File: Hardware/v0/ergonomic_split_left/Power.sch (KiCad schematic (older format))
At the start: 3 parts, among them U9 TCR2EF33

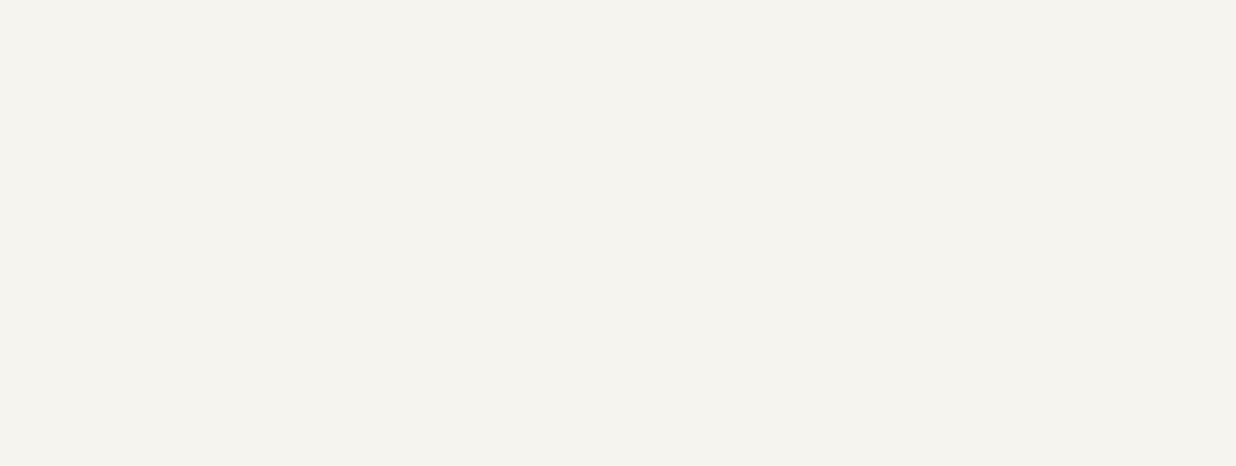
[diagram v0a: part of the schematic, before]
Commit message: Drawing board outline Basic placement done Adding rotary encoder to the switch matrix Adding mounting holes
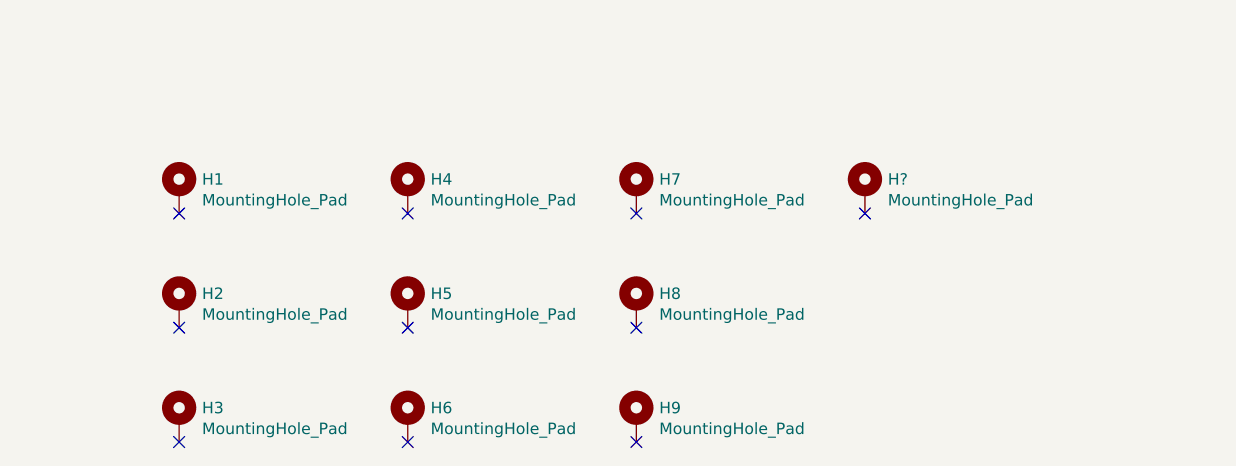
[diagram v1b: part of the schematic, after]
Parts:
- added H1, H2, H3, H4, H5, H6, H7, H8, H9, H?: MountingHole_Pad, mounting_hole:MountingHole_3.2mm_M3_ISO7380_Pad, symbol Mechanical:MountingHole_Pad
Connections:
- no-connect marks 0 -> 10
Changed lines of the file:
@@
 $Descr A4 11693 8268
 encoding utf-8
-Sheet 7 7
+Sheet 6 7
 Title "TKL Keyboard"
 Date ""
@@
 	1    0    0    -1
 $EndComp
+$Comp
+L Mechanical:MountingHole_Pad H1
+U 1 1 62F25DCF
+P 1500 5550
+F 0 "H1" H 1600 5599 50  0000 L CNN
+F 1 "MountingHole_Pad" H 1600 5508 50  0000 L CNN
+F 2 "mounting_hole:MountingHole_3.2mm_M3_ISO7380_Pad" H 1500 5550 50  0001 C CNN
+F 3 "~" H 1500 5550 50  0001 C CNN
+	1    1500 5550
+	1    0    0    -1
+$EndComp
+NoConn ~ 1500 5650
+$Comp
+L Mechanical:MountingHole_Pad H2
+U 1 1 62F281A1
+P 1500 6050
+F 0 "H2" H 1600 6099 50  0000 L CNN
+F 1 "MountingHole_Pad" H 1600 6008 50  0000 L CNN
+F 2 "mounting_hole:MountingHole_3.2mm_M3_ISO7380_Pad" H 1500 6050 50  0001 C CNN
+F 3 "~" H 1500 6050 50  0001 C CNN
+	1    1500 6050
+	1    0    0    -1
+$EndComp
+NoConn ~ 1500 6150
+$Comp
+L Mechanical:MountingHole_Pad H3
+U 1 1 62F28C3F
+P 1500 6550
+F 0 "H3" H 1600 6599 50  0000 L CNN
+F 1 "MountingHole_Pad" H 1600 6508 50  0000 L CNN
+F 2 "mounting_hole:MountingHole_3.2mm_M3_ISO7380_Pad" H 1500 6550 50  0001 C CNN
+F 3 "~" H 1500 6550 50  0001 C CNN
+	1    1500 6550
+	1    0    0    -1
+$EndComp
+NoConn ~ 1500 6650
+$Comp
+L Mechanical:MountingHole_Pad H4
+U 1 1 62F2B314
+P 2500 5550
+F 0 "H4" H 2600 5599 50  0000 L CNN
+F 1 "MountingHole_Pad" H 2600 5508 50  0000 L CNN
+F 2 "mounting_hole:MountingHole_3.2mm_M3_ISO7380_Pad" H 2500 5550 50  0001 C CNN
+F 3 "~" H 2500 5550 50  0001 C CNN
+	1    2500 5550
+	1    0    0    -1
+$EndComp
+NoConn ~ 2500 5650
+$Comp
+L Mechanical:MountingHole_Pad H5
+U 1 1 62F2B31B
+P 2500 6050
+F 0 "H5" H 2600 6099 50  0000 L CNN
+F 1 "MountingHole_Pad" H 2600 6008 50  0000 L CNN
+F 2 "mounting_hole:MountingHole_3.2mm_M3_ISO7380_Pad" H 2500 6050 50  0001 C CNN
+F 3 "~" H 2500 6050 50  0001 C CNN
+	1    2500 6050
+	1    0    0    -1
+$EndComp
+NoConn ~ 2500 6150
+$Comp
+L Mechanical:MountingHole_Pad H6
+U 1 1 62F2B322
+P 2500 6550
+F 0 "H6" H 2600 6599 50  0000 L CNN
+F 1 "MountingHole_Pad" H 2600 6508 50  0000 L CNN
+F 2 "mounting_hole:MountingHole_3.2mm_M3_ISO7380_Pad" H 2500 6550 50  0001 C CNN
+F 3 "~" H 2500 6550 50  0001 C CNN
+	1    2500 6550
+	1    0    0    -1
+$EndComp
+NoConn ~ 2500 6650
+$Comp
+L Mechanical:MountingHole_Pad H7
+U 1 1 62F2BF2F
+P 3500 5550
+F 0 "H7" H 3600 5599 50  0000 L CNN
+F 1 "MountingHole_Pad" H 3600 5508 50  0000 L CNN
+F 2 "mounting_hole:MountingHole_3.2mm_M3_ISO7380_Pad" H 3500 5550 50  0001 C CNN
+F 3 "~" H 3500 5550 50  0001 C CNN
+	1    3500 5550
+	1    0    0    -1
+$EndComp
+NoConn ~ 3500 5650
+$Comp
+L Mechanical:MountingHole_Pad H8
+U 1 1 62F2BF36
+P 3500 6050
+F 0 "H8" H 3600 6099 50  0000 L CNN
+F 1 "MountingHole_Pad" H 3600 6008 50  0000 L CNN
+F 2 "mounting_hole:MountingHole_3.2mm_M3_ISO7380_Pad" H 3500 6050 50  0001 C CNN
+F 3 "~" H 3500 6050 50  0001 C CNN
+	1    3500 6050
+	1    0    0    -1
+$EndComp
+NoConn ~ 3500 6150
+$Comp
+L Mechanical:MountingHole_Pad H9
+U 1 1 62F2BF3D
+P 3500 6550
+F 0 "H9" H 3600 6599 50  0000 L CNN
+F 1 "MountingHole_Pad" H 3600 6508 50  0000 L CNN
+F 2 "mounting_hole:MountingHole_3.2mm_M3_ISO7380_Pad" H 3500 6550 50  0001 C CNN
+F 3 "~" H 3500 6550 50  0001 C CNN
+	1    3500 6550
+	1    0    0    -1
+$EndComp
+NoConn ~ 3500 6650
+$Comp
+L Mechanical:MountingHole_Pad H?
+U 1 1 629C12E0
+P 4500 5550
+F 0 "H?" H 4600 5599 50  0000 L CNN
+F 1 "MountingHole_Pad" H 4600 5508 50  0000 L CNN
+F 2 "mounting_hole:MountingHole_3.2mm_M3_ISO7380_Pad" H 4500 5550 50  0001 C CNN
+F 3 "~" H 4500 5550 50  0001 C CNN
+	1    4500 5550
+	1    0    0    -1
+$EndComp
+NoConn ~ 4500 5650
 $EndSCHEMATC

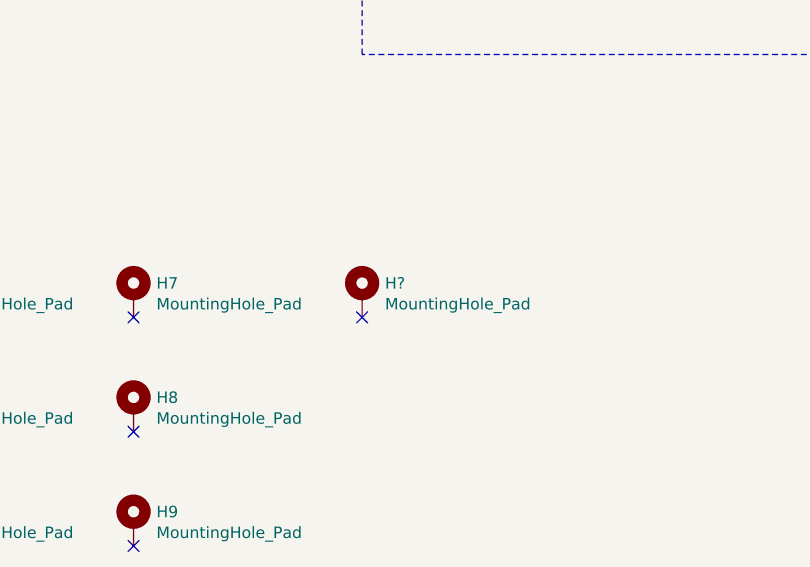
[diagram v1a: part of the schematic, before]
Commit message: Adding power and ground planes Adding right interface USB C connector Pin swapping on ATMEGA
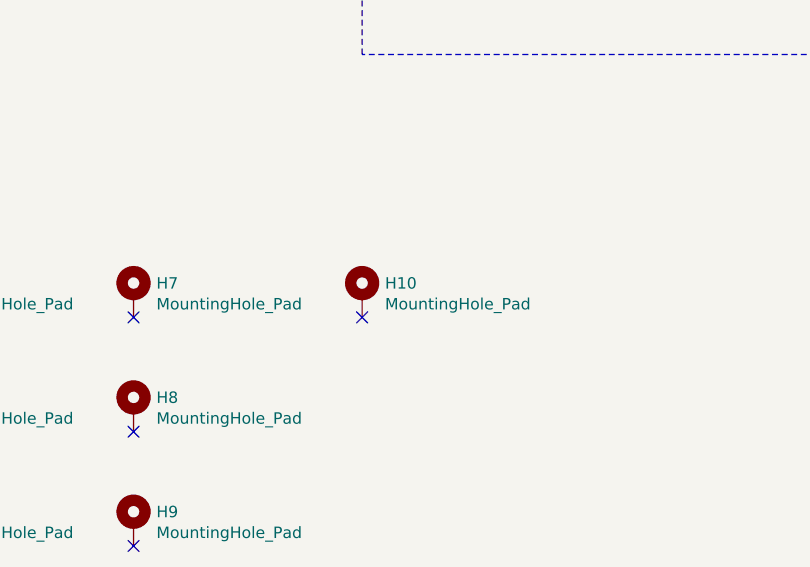
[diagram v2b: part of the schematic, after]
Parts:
- gave numbers to parts that had none: 1
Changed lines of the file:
@@
 NoConn ~ 3500 6650
 $Comp
-L Mechanical:MountingHole_Pad H?
+L Mechanical:MountingHole_Pad H10
 U 1 1 629C12E0
 P 4500 5550
-F 0 "H?" H 4600 5599 50  0000 L CNN
+F 0 "H10" H 4600 5599 50  0000 L CNN
 F 1 "MountingHole_Pad" H 4600 5508 50  0000 L CNN
 F 2 "mounting_hole:MountingHole_3.2mm_M3_ISO7380_Pad" H 4500 5550 50  0001 C CNN
